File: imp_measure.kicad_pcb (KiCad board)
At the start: 2 copper layers, 89.4 x 42.9 mm, 61 parts, among them IC1 DAC80501ZDGST, IC2 MAX660MX_NOPB, IC4 MC33202DR2G, J1 Conn_01x04_Pin, J2 USB_B_Micro, J3 Conn_01x04_Pin, J4 Conn_01x06_Pin, J5 Conn_01x04_Pin, SW1 SW_SPDT, U1 AMS1117-3.3, U2 STM32F401RCTx, Y1 Crystal

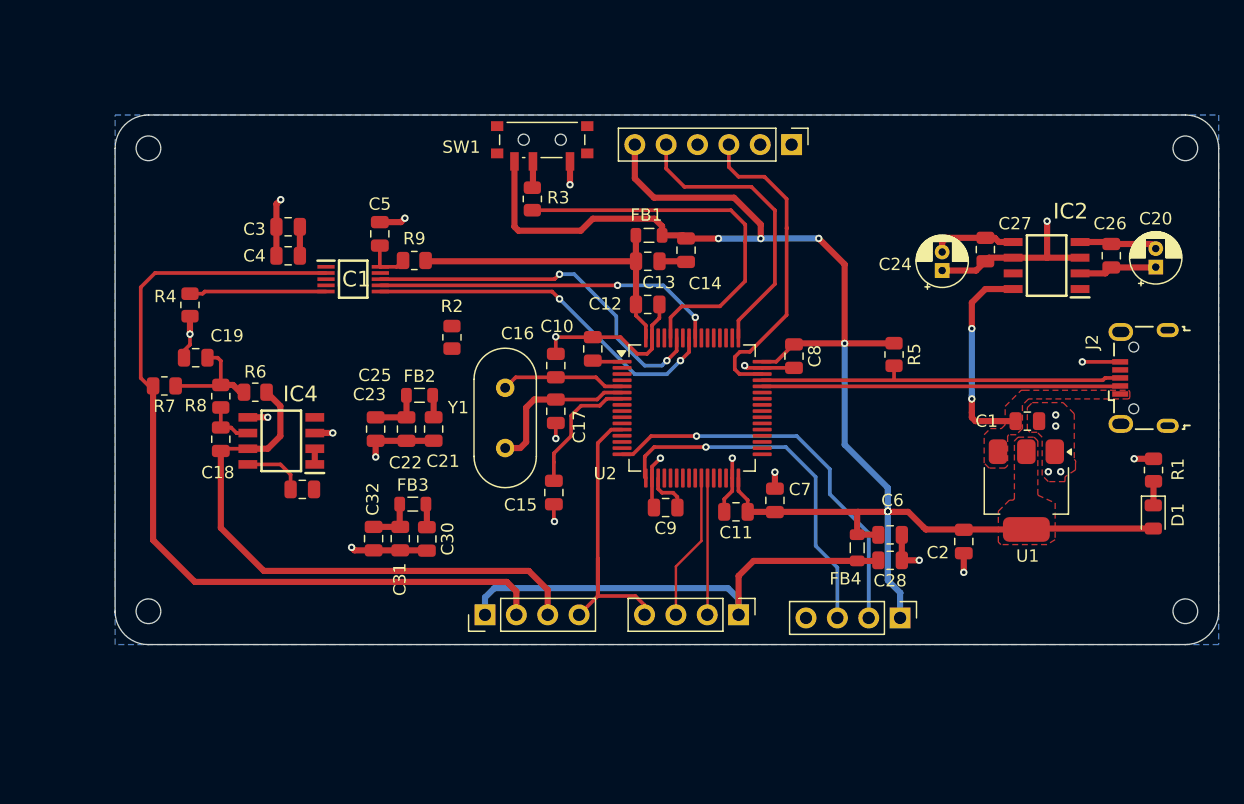
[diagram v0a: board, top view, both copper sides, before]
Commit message: Ground fill for analog part
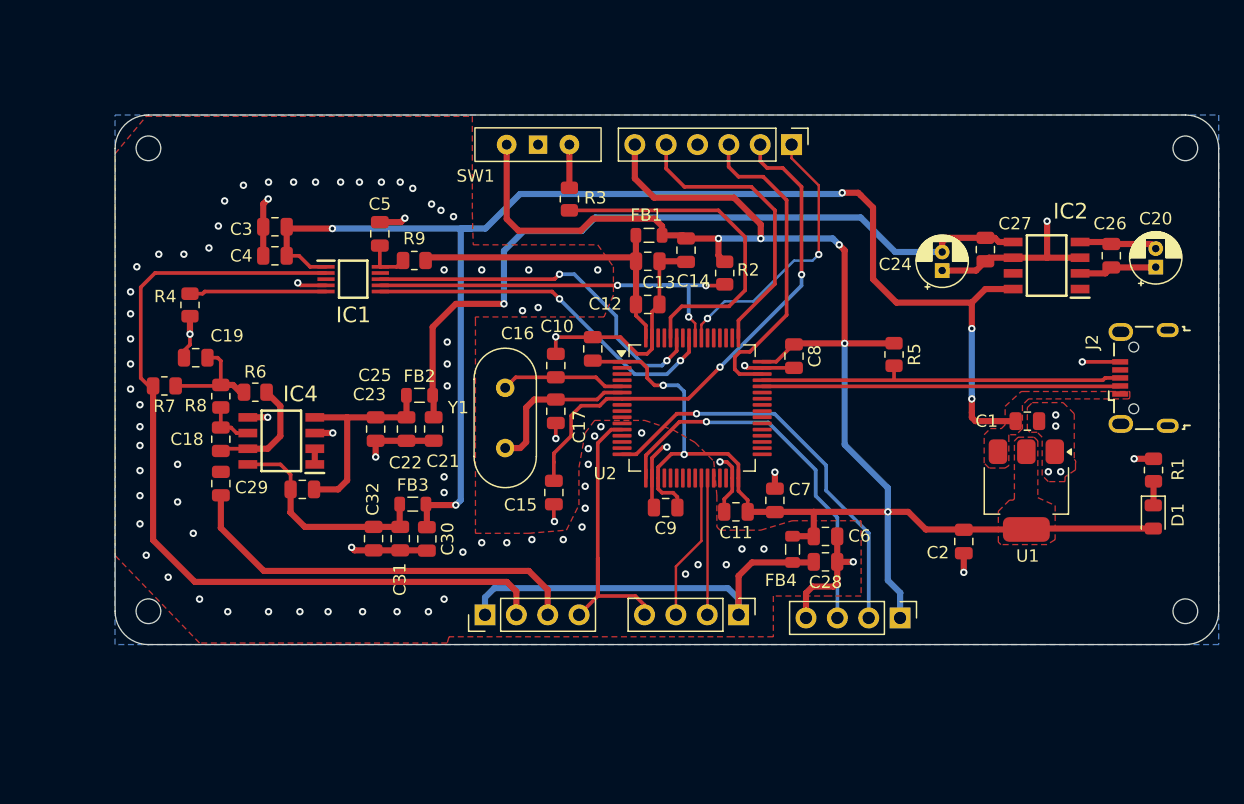
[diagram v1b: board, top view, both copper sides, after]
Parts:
- added C29: 1n, Capacitor_SMD:C_0805_2012Metric, F.Cu at (105.9, 87.2)
- C18: value 5n -> 1n
- C19: value 10n -> 1n
- C5: value 100n -> 330n
- R9: value 10k -> 1k
- SW1: footprint Button_Switch_SMD:SW_SPDT_PCM12 -> Button_Switch_THT:SW_Slide-03_Wuerth-WS-SLTV_10x2.5x6.4_P2.54mm
- U2: value STM32F401RCTx -> STM32F401RCT6
- moved R2 22.7 mm to (146.7, 70.1)
- moved C28 5.24 mm to (154.8, 93.5)
- moved C6 5.24 mm to (154.8, 91.4)
- moved FB4 5.24 mm to (152.2, 92.5)
- moved R3 3.00 mm to (134.1, 64.1)
- moved C3 1.07 mm to (110.2, 66.4)
- moved C4 1.07 mm to (110.2, 68.7)
- moved SW1 0.35 mm to (131.6, 59.7)
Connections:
- C18 pad 2: /DAC_OUT_FILTERED -> Net-(C18-Pad2)
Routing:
- net VBUS: track 21.0 -> 114.1 mm, vias 2 -> 5
- net VBUS_M: track 8.65 -> 62.8 mm, vias 0 -> 1
- net /NRST: track 10.6 -> 42.4 mm, vias 0 -> 2
- net +3.3V: track 137.7 -> 163.2 mm, vias 8 -> 7
- net /SYS_JTDO_SWO: track 0.00 -> 22.7 mm, vias 0 -> 2
- net VBUS_MF: track 4.29 -> 17.3 mm
- net GND: track 109.4 -> 121.9 mm, vias 24 -> 96
- net VBUS_PF: track 9.03 -> 18.1 mm
- net /SPI1_NSS: track 28.3 -> 34.5 mm, vias 2 -> 3
- net +3.3V_F: track 38.9 -> 33.6 mm
- net /DAC_OUT_FILTERED: track 46.2 -> 42.6 mm
- net Net-(U2-BOOT0): track 31.2 -> 28.1 mm
- net /USART2_RX: track 29.1 -> 31.1 mm
- net /USART2_TX: track 31.9 -> 33.4 mm
- net Net-(SW1-B): track 2.22 -> 3.53 mm
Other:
- outline, holes or cut-outs redrawn

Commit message: PCB v1.2
Changing the Multiple Feedback topology to Salen-Key.
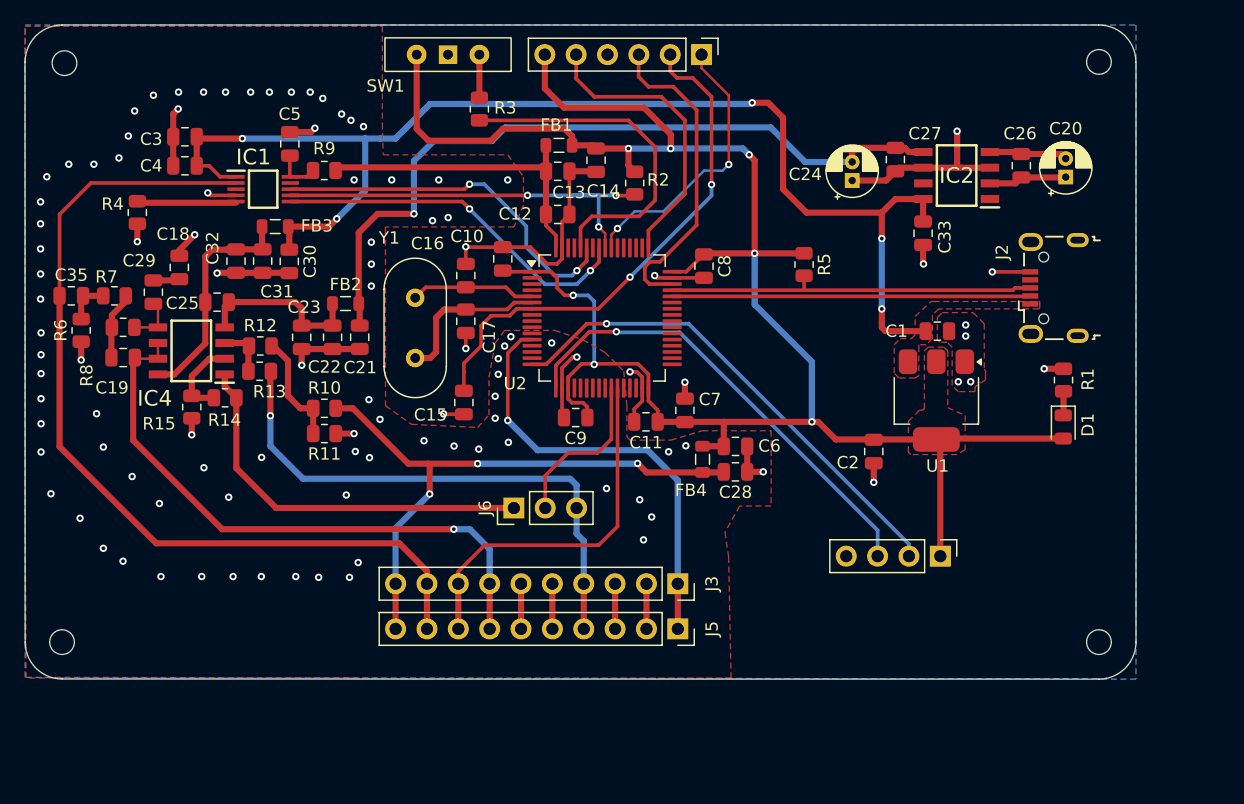
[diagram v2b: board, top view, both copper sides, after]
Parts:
- added C33: 1u, Capacitor_SMD:C_0805_2012Metric, F.Cu at (162.8, 66.9)
- added C35: 10u, Capacitor_SMD:C_0805_2012Metric, F.Cu at (93.8, 72.0)
- added J6: Conn_01x03_Pin, Connector_PinHeader_2.54mm:PinHeader_1x03_P2.54mm_Vertical, F.Cu at (129.6, 89.1)
- added R10: 1k, Resistor_SMD:R_0805_2012Metric, F.Cu at (114.3, 81.1)
- added R11: 1k, Resistor_SMD:R_0805_2012Metric, F.Cu at (114.3, 83.1)
- added R12: 10M, Resistor_SMD:R_0805_2012Metric, F.Cu at (109.1, 76.0)
- added R13: 10M, Resistor_SMD:R_0805_2012Metric, F.Cu at (109.0, 78.1)
- added R14: 10M, Resistor_SMD:R_0805_2012Metric, F.Cu at (106.2, 80.2)
- added R15: 10M, Resistor_SMD:R_0805_2012Metric, F.Cu at (103.5, 81.0)
- J3, J5: value Conn_01x04_Pin -> Conn_01x10_Pin; footprint Connector_PinHeader_2.54mm:PinHeader_1x04_P2.54mm_Vertical -> Connector_PinSocket_2.54mm:PinSocket_1x10_P2.54mm_Vertical
- R6: value 3k3 -> 10k
- R7: value 3k3 -> 5k
- R8: value 1k6 -> 1k
- R9: value 1k -> 1k5
- moved FB3 25.1 mm to (110.3, 66.3)
- moved C30 25.1 mm to (111.4, 69.2)
- moved C31 25.1 mm to (109.3, 69.1)
- moved C32 25.1 mm to (107.1, 69.1)
- moved C25 16.7 mm to (105.6, 72.5)
- moved C29 16.4 mm to (100.4, 71.7)
- moved J5 15.7 mm to (142.9, 98.9), turned to -90 degrees
- moved R6 15.0 mm to (94.5, 74.8), turned to 90 degrees
- moved C18 14.3 mm to (102.5, 69.7)
- moved C14 10.3 mm to (136.3, 61.0)
- moved C15 10.3 mm to (125.6, 80.6)
- moved C24 10.3 mm to (157.0, 62.6)
- moved C27 10.3 mm to (160.5, 60.9)
- moved D1 10.3 mm to (174.1, 82.6)
- moved R5 10.3 mm to (153.1, 69.4)
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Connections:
- C18 pad 1: Net-(IC4-INPUTS_2_2) -> GND
- C19 pad 2: GND -> /DAC_OUT_FILTERED
- C29 pad 2: /DAC_OUT_FILTERED -> Net-(IC4-INPUTS_2_1)
- IC4 pad 1: Net-(IC4-INPUTS_1_1) -> /ADC_IN4_MID
- IC4 pad 3: GND -> Net-(IC4-INPUTS_1_2)
- IC4 pad 5: GND -> Net-(IC4-INPUTS_2_1)
- IC4 pad 6: Net-(IC4-INPUTS_2_2) -> /DAC_OUT_FILTERED
- J3 pad 1: +3.3V_F -> GND
- J3 pad 2: /ADC1_IN5 -> /IMP3
- J3 pad 3: /ADC1_IN4 -> /IMP4
- J3 pad 4: GND -> /ADC1_IN4_SIGNAL
- J5 pad 1: +3.3V_F -> GND
- J5 pad 2: /DAC_OUT -> /IMP3
- J5 pad 3: /DAC_OUT_FILTERED -> /IMP4
- J5 pad 4: GND -> /ADC1_IN4_SIGNAL
- R6 pad 1: Net-(C19-Pad1) -> GND
- R6 pad 2: /DAC_OUT_FILTERED -> Net-(C35-Pad2)
- R7 pad 1: /DAC_OUT -> Net-(C35-Pad2)
- R8 pad 2: Net-(IC4-INPUTS_2_2) -> Net-(IC4-INPUTS_2_1)
- U2 pad 26: /ADC1_IN4 -> /ADC_IN4
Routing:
- net /ADC1_IN4_SIGNAL: track 0.00 -> 44.1 mm, vias 0 -> 1
- net /ADC_IN4_MID: track 0.00 -> 31.8 mm
- net /ADC1_IN5: track 11.1 -> 30.3 mm
- net +3.3V_F: track 33.6 -> 48.0 mm, vias 0 -> 3
- net /ADC_IN4: track 0.00 -> 13.3 mm
- net VBUS: track 114.1 -> 101.9 mm
- net /ADC1_IN4: track 11.9 -> 0.00 mm
- net /VF_MID: track 0.00 -> 9.19 mm
- net /USART2_TX: track 33.4 -> 40.3 mm
- net /USART2_RX: track 31.1 -> 37.8 mm
- net GND: track 121.9 -> 128.4 mm, vias 96 -> 107
- net /DAC_OUT_FILTERED: track 42.6 -> 48.9 mm, vias 0 -> 1
- net Net-(IC4-INPUTS_1_1): track 1.27 -> 6.71 mm
- net Net-(IC4-INPUTS_1_2): track 0.00 -> 4.14 mm
- net Net-(IC4-INPUTS_2_2): track 4.00 -> 0.00 mm
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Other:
- board size 89.4 x 42.9 mm -> 90 x 53 mm

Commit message: Forrasztáshoz
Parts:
- added J7: Conn_01x10_Pin, Connector_PinSocket_2.54mm:PinSocket_1x10_P2.54mm_Vertical, F.Cu at (142.9, 108.0)
- added J8: Conn_01x03_Pin, Connector_PinHeader_2.54mm:PinHeader_1x03_P2.54mm_Vertical, F.Cu at (122.6, 97.0)
- moved H3 8.00 mm to (93.0, 108.0)
- moved H4 8.00 mm to (177.0, 108.0)
- moved J3 5.40 mm to (142.9, 100.7)
- moved J5 5.40 mm to (142.9, 104.3)
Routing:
- net /ADC1_IN5: track 30.3 -> 39.3 mm
- net /DAC_OUT_FILTERED: track 48.9 -> 58.0 mm
- net /DAC_OUT: track 72.8 -> 81.9 mm
- net +3.3V_F: track 48.0 -> 57.1 mm
- net GND: track 128.4 -> 137.5 mm
- net /ADC1_IN4_SIGNAL: track 44.1 -> 53.2 mm
- net /IMP3: track 3.70 -> 7.37 mm
- net /IMP1: track 3.66 -> 7.33 mm
- net /IMP4: track 3.66 -> 7.33 mm
- net /IMP2: track 3.66 -> 7.33 mm
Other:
- board size 90 x 53 mm -> 90 x 61 mm
